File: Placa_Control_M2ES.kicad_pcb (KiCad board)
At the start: 2 copper layers, 204 x 108 mm, 311 parts, among them J1 Screw_Terminal_01x06, J10 Screw_Terminal_01x06, J11 Screw_Terminal_01x02, J12 7499010211A, J13 Screw_Terminal_01x04, J2 Screw_Terminal_01x06, J3 Screw_Terminal_01x06, J4 Screw_Terminal_01x06, J5 Screw_Terminal_01x06, J6 Screw_Terminal_01x06, J7 Screw_Terminal_01x06, J8 Screw_Terminal_01x06, J9 Screw_Terminal_01x06, K1 HF46F-G, K10 HF46F-G, K11 HF46F-G, K12 HF46F-G, K2 HF46F-G, K3 HF46F-G, K4 HF46F-G, K5 HF46F-G, K6 HF46F-G, K7 HF46F-G, K8 HF46F-G, K9 HF46F-G, U1 ULN2003, U10 L78M08CDT-TR, U11 LD29150, U12 LAN8742A, U13 USBLC6-4SC6, U14 TLV9101, U15 TLV9101, U16 TLV9101, U17 TLV9101, U18 TLV9101, U19 TLV9101, U2 ULN2003, U20 TLV9101, U21 TLV9101, U22 REF3030, U23 STM32H743VITx, U3 REF35102QDBVR, U4 ADS1256, U5 ADS1256, U6 TLV9101, U7 OKI-78SR-12_1.0-W36-C, U8 uA7810, U9 LD29150, Y1 8.0Mhz, Y2 8.0Mhz, Y3 25Mhz, Y4 8Mhz

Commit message: Avance del posicionamiento
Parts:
- removed J7: Screw_Terminal_01x06, LIB_PCB_CONT:15EDGVC_6P_3.81mm_Male-Vert_Degson
- moved R60 283.1 mm to (242.6, 83.1), turned to 180 degrees
- moved R61 281.1 mm to (242.6, 81.5), turned to 0 degrees
- moved D3 278.6 mm to (237.5, 82.2), turned to 0 degrees
- moved C66 277.4 mm to (233.4, 79.8), turned to 180 degrees
- moved R64 271.2 mm to (240.2, 82.3), turned to -90 degrees
- moved U14 270.8 mm to (233.4, 82.1), turned to 0 degrees
- moved R62 267.2 mm to (230.5, 80.5), turned to -90 degrees
- moved R63 263.9 mm to (230.5, 83.7)
- moved D4 262.8 mm to (228.7, 83.8), turned to -90 degrees
- moved R65 261.5 mm to (233.2, 84.4), turned to 0 degrees
- moved R66 255.8 mm to (228.7, 80.6), turned to -90 degrees
- moved C13 193.3 mm to (170.7, 54.7)
- moved C14 189.3 mm to (171.8, 59.1), turned to 0 degrees
- moved U4 177.7 mm to (164.0, 57.6), turned to -90 degrees
- moved C9 177.3 mm to (157.2, 60.5)
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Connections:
- J5 pad 2: /Digital Inputs/NAMUR_1 -> /8V
- J5 pad 3: /8V -> GND
- J5 pad 4: /Digital Inputs/NAMUR_2 -> /Digital Inputs/NAMUR_1
- J5 pad 5: /8V -> /Digital Inputs/NAMUR_2
- J6 pad 1: /8V -> /Digital Inputs/NAMUR_4
- J6 pad 2: /Digital Inputs/NAMUR_4 -> /Digital Inputs/NAMUR_5
- J6 pad 3: /8V -> /Digital Inputs/NAMUR_6
- J6 pad 4: /Digital Inputs/NAMUR_5 -> /Digital Inputs/NAMUR_7
- J6 pad 5: /8V -> /Digital Inputs/NAMUR_8
- J6 pad 6: /Digital Inputs/NAMUR_6 -> /Digital Inputs/NAMUR_9

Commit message: Se empieza a evaluar la conexión del ethernet con la carcasa, parte analog, dig y micro en posición, tambien se busca solución para la salida de led de las entradas digitales
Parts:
- removed C74: 100nF/50V, Capacitor_SMD:C_0603_1608Metric
- removed J12: 7499010211A, Connector_RJ:RJ45_Wuerth_7499010211A_Horizontal
- added J7: ARJM11C7-009-AB-EW2, LIB_PCB_CONT:ARJM11C7-009-AB-EW2_Abracon, F.Cu at (238.5, 44.1)
- C57: value 10uF/50V -> 1uF/50V
- C60: value 10nF/50V -> 100nF/50V
- moved R74 299.0 mm to (242.3, 104.5), turned to 180 degrees
- moved D15 298.1 mm to (239.0, 125.8), turned to -90 degrees
- moved D7 297.2 mm to (239.1, 104.1), turned to -90 degrees
- moved R106 297.0 mm to (242.4, 127.8), turned to 0 degrees
- moved R102 297.0 mm to (242.4, 126.2)
- moved R103 297.0 mm to (242.4, 124.6), turned to 0 degrees
- moved R75 296.5 mm to (242.3, 102.9), turned to 0 degrees
- moved U20 294.6 mm to (235.8, 125.6), turned to 90 degrees
- moved C68 292.9 mm to (233.7, 103.6), turned to -90 degrees
- moved D16 291.4 mm to (232.8, 127.8)
- moved U16 289.9 mm to (235.9, 103.9)
- moved D5 289.1 mm to (239.1, 98.7), turned to -90 degrees
- moved R78 289.0 mm to (242.3, 106.1), turned to 0 degrees
- moved C72 288.3 mm to (233.6, 125.3), turned to -90 degrees
- moved R67 287.7 mm to (242.3, 99.0)
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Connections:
- J5 pad 1: /8V -> /Digital Inputs/NAMUR_6
- J5 pad 2: /8V -> /Digital Inputs/NAMUR_5
- J5 pad 3: GND -> /Digital Inputs/NAMUR_4
- J5 pad 4: /Digital Inputs/NAMUR_1 -> /Digital Inputs/NAMUR_3
- J5 pad 6: /Digital Inputs/NAMUR_3 -> /Digital Inputs/NAMUR_1
- J6 pad 1: /Digital Inputs/NAMUR_4 -> /8V
- J6 pad 2: /Digital Inputs/NAMUR_5 -> GND
- J6 pad 3: /Digital Inputs/NAMUR_6 -> unconnected-(J6-Pin_3-Pad3)
- J6 pad 4: /Digital Inputs/NAMUR_7 -> /Digital Inputs/NAMUR_9
- J6 pad 6: /Digital Inputs/NAMUR_9 -> /Digital Inputs/NAMUR_7
- U23 pad 1: /Digital Inputs/DIG_9 -> unconnected-(U23-PE2-Pad1)
- U23 pad 46: unconnected-(U23-PB10-Pad46) -> /Analog Inputs/ADS_SCLK
- U23 pad 53: unconnected-(U23-PB14-Pad53) -> /Analog Inputs/ADS_MISO
- U23 pad 54: unconnected-(U23-PB15-Pad54) -> /Analog Inputs/ADS_MOSI
- U23 pad 55: unconnected-(U23-PD8-Pad55) -> /Analog Inputs/ADS2_DRDY
- U23 pad 56: unconnected-(U23-PD9-Pad56) -> /Analog Inputs/ADS2_CS
- U23 pad 57: unconnected-(U23-PD10-Pad57) -> /Analog Inputs/ADS1_DRDY
- U23 pad 58: unconnected-(U23-PD11-Pad58) -> /Analog Inputs/ADS1_CS
- U23 pad 60: /Digital Outputs/Relay_1 -> /Digital Outputs/Relay_12
- U23 pad 61: /Digital Outputs/Relay_2 -> /Digital Outputs/Relay_11
- U23 pad 62: /Digital Outputs/Relay_3 -> /Digital Outputs/Relay_10
- U23 pad 63: /Digital Outputs/Relay_4 -> /Digital Outputs/Relay_9
- U23 pad 64: /Digital Outputs/Relay_5 -> /Digital Outputs/Relay_8
- U23 pad 65: /Digital Outputs/Relay_6 -> /Digital Outputs/Relay_7
- U23 pad 66: /Digital Outputs/Relay_7 -> /Digital Outputs/Relay_6
- U23 pad 67: /Digital Outputs/Relay_8 -> /Digital Outputs/Relay_5
- U23 pad 68: /Digital Outputs/Relay_9 -> /Digital Outputs/Relay_4
- U23 pad 69: /Digital Outputs/Relay_10 -> /Digital Outputs/Relay_3
- U23 pad 70: /Digital Outputs/Relay_11 -> /Digital Outputs/Relay_2
- U23 pad 71: /Digital Outputs/Relay_12 -> /Digital Outputs/Relay_1
- U23 pad 78: /Analog Inputs/ADS_SCLK -> unconnected-(U23-PC10-Pad78)
- U23 pad 79: /Analog Inputs/ADS_MISO -> unconnected-(U23-PC11-Pad79)
- U23 pad 80: /Analog Inputs/ADS_MOSI -> unconnected-(U23-PC12-Pad80)
- U23 pad 83: /Analog Inputs/ADS1_DRDY -> unconnected-(U23-PD2-Pad83)
- U23 pad 84: /Analog Inputs/ADS1_CS -> /Digital Inputs/DIG_9
- U23 pad 85: /Analog Inputs/ADS2_DRDY -> /Digital Inputs/DIG_8
- U23 pad 86: /Analog Inputs/ADS2_CS -> /Digital Inputs/DIG_7
- U23 pad 87: unconnected-(U23-PD6-Pad87) -> /Digital Inputs/DIG_6
- U23 pad 90: /Digital Inputs/DIG_1 -> /Digital Inputs/DIG_5
- U23 pad 91: /Digital Inputs/DIG_2 -> /Digital Inputs/DIG_4
- U23 pad 93: /Digital Inputs/DIG_4 -> unconnected-(U23-PB7-Pad93)
- U23 pad 95: /Digital Inputs/DIG_5 -> unconnected-(U23-PB8-Pad95)
- U23 pad 96: /Digital Inputs/DIG_6 -> /Digital Inputs/DIG_2
- U23 pad 97: /Digital Inputs/DIG_7 -> /Digital Inputs/DIG_1
- U23 pad 98: /Digital Inputs/DIG_8 -> unconnected-(U23-PE1-Pad98)
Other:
- outline, holes or cut-outs redrawn

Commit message: Se traza vcc, digital, analog, relay, esta por terminar corregir GND y revisar nuevamente
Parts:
- removed D10, D12, D14, D16, D18, D2, D4, D6, D8: LED, LED_SMD:LED_0603_1608Metric
- removed R101, R108, R115, R66, R73, R80, R87, R9, R94: 2k2, Resistor_SMD:R_0603_1608Metric
- moved J13 139.4 mm to (177.3, 91.1)
- moved JP1 105.1 mm to (211.2, 75.9), turned to 180 degrees
- moved C76 90.9 mm to (211.3, 78.2), turned to 0 degrees
- moved C53 82.9 mm to (230.3, 78.4), turned to 180 degrees
- moved FB1 75.5 mm to (226.5, 65.9), turned to 180 degrees
- moved C55 58.6 mm to (230.5, 76.6), turned to 180 degrees
- moved C56 57.5 mm to (235.9, 75.7), turned to -90 degrees
- moved R47 18.8 mm to (202.1, 63.2), turned to 180 degrees
- moved C5 18.6 mm to (87.7, 66.6), turned to 90 degrees
- moved R39 18.3 mm to (190.6, 61.9)
- moved R44 18.3 mm to (189.0, 61.9)
- moved R55 17.9 mm to (229.3, 58.3), turned to 180 degrees
- moved R41 17.2 mm to (202.1, 64.9), turned to 0 degrees
- moved R45 16.5 mm to (202.1, 66.5), turned to 180 degrees
- moved R40 16.4 mm to (197.8, 61.9)
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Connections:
- C20 pad 1: Net-(PS1-AC/L) -> Net-(J11-Pin_1)
- C20 pad 2: Net-(J11-Pin_2) -> Net-(PS1-AC/N)
- F1 pad 1: Net-(J11-Pin_1) -> Net-(J11-Pin_2)
- F1 pad 2: Net-(PS1-AC/L) -> Net-(PS1-AC/N)
- J7 pad S1: Net-(J7-PadS1) -> unconnected-(J7-PadS1)_1
- J7 pad S2: Net-(J7-PadS1) -> unconnected-(J7-PadS1)
- PS1 pad 1: Net-(J11-Pin_2) -> Net-(PS1-AC/N)
- PS1 pad 2: Net-(PS1-AC/L) -> Net-(J11-Pin_1)
- RV1 pad 1: Net-(PS1-AC/L) -> Net-(J11-Pin_1)
- RV1 pad 2: Net-(J11-Pin_2) -> Net-(PS1-AC/N)
- U23 pad 55: /Analog Inputs/ADS2_DRDY -> /Analog Inputs/ADS1_DRDY
- U23 pad 56: /Analog Inputs/ADS2_CS -> /Analog Inputs/ADS1_CS
- U23 pad 57: /Analog Inputs/ADS1_DRDY -> /Analog Inputs/ADS2_DRDY
- U23 pad 58: /Analog Inputs/ADS1_CS -> /Analog Inputs/ADS2_CS
- U23 pad 81: unconnected-(U23-PD0-Pad81) -> /Digital Inputs/DIG_9
- U23 pad 82: unconnected-(U23-PD1-Pad82) -> /Digital Inputs/DIG_8
- U23 pad 83: unconnected-(U23-PD2-Pad83) -> /Digital Inputs/DIG_7
- U23 pad 84: /Digital Inputs/DIG_9 -> /Digital Inputs/DIG_6
- U23 pad 85: /Digital Inputs/DIG_8 -> unconnected-(U23-PD4-Pad85)
- U23 pad 86: /Digital Inputs/DIG_7 -> unconnected-(U23-PD5-Pad86)
- U23 pad 87: /Digital Inputs/DIG_6 -> unconnected-(U23-PD6-Pad87)
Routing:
- net /3V3: track 0.00 -> 541.4 mm, vias 0 -> 33
- net /24V: track 0.00 -> 335.9 mm
- net /8V: track 0.00 -> 188.1 mm, vias 0 -> 4
- net /5V: track 0.00 -> 154.1 mm, vias 0 -> 3
- net GND: track 0.00 -> 134.0 mm, vias 0 -> 53
- net /Ethernet/ETH_TXD1: track 0.00 -> 128.7 mm, vias 0 -> 2
- net /Ethernet/ETH_TXD0: track 0.00 -> 123.6 mm, vias 0 -> 2
- net /10V: track 0.00 -> 107.2 mm
- net /Ethernet/ETH_TX_EN: track 0.00 -> 106.3 mm, vias 0 -> 2
- net /Digital Inputs/DIG_9: track 0.00 -> 91.8 mm
- net /Fuente/12V: track 0.00 -> 91.7 mm
- net /Digital Inputs/DIG_8: track 0.00 -> 86.8 mm
- net /Analog Inputs/REF_2.5V: track 0.00 -> 85.7 mm, vias 0 -> 3
- net /Digital Inputs/DIG_7: track 0.00 -> 80.7 mm
- net /Ethernet/ETH_MDIO: track 0.00 -> 80.6 mm
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- added copper zone on B.Cu, net GND
- added copper zone on F.Cu, net GND
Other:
- outline, holes or cut-outs redrawn

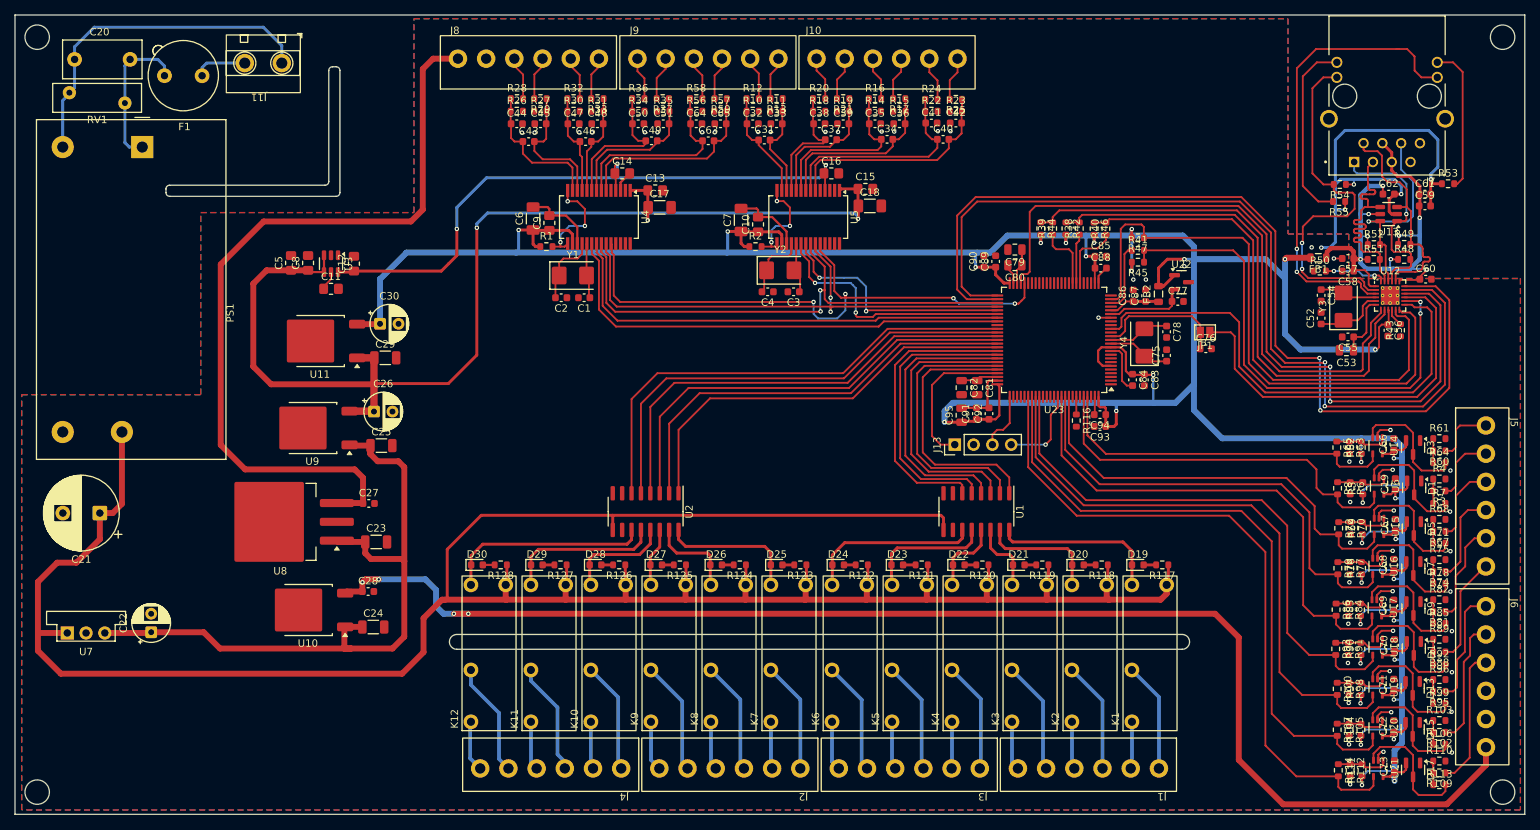
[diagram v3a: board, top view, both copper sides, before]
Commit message: Se termina de revisar la placa. Se corrige la terminación de los transformadores internos del puerto ethernet. Se revisa GND, espaciado, añadimos notas. Falta enlazar las partes de JLCPCN
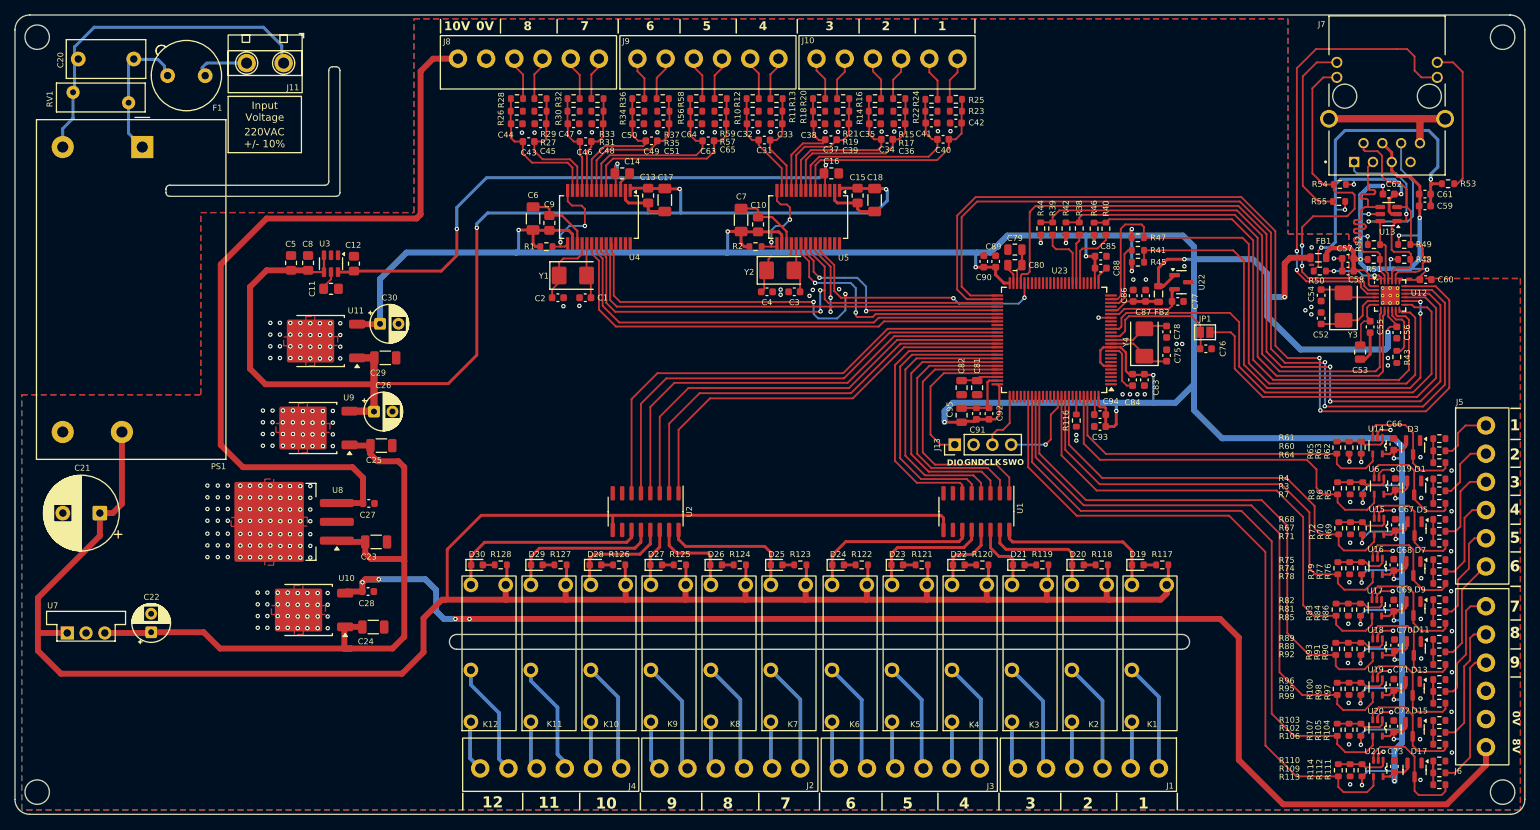
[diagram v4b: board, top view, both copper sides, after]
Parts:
- moved R43 3.63 mm to (237.1, 79.3)
- moved C55 3.29 mm to (233.5, 75.2), turned to -90 degrees
- moved C53 1.87 mm to (232.1, 78.6), turned to -90 degrees
- moved C15 1.38 mm to (164.2, 57.5), turned to -90 degrees
- moved C56 1.24 mm to (237.1, 76.0)
- moved C17 1.22 mm to (138.2, 58.1), turned to -90 degrees
- moved C13 1.18 mm to (135.9, 57.5), turned to -90 degrees
- moved C18 1.03 mm to (166.5, 58.1), turned to -90 degrees
- moved C20 0.50 mm to (58.9, 39.0)
- moved RV1 0.50 mm to (58.2, 43.5)
- moved C2 0.45 mm to (123.7, 71.3)
- moved F1 0.42 mm to (76.1, 41.3)
- moved J11 0.25 mm to (89.2, 35.8)
- moved D17 0.20 mm to (239.5, 135.1)
- moved C1 0.15 mm to (127.4, 71.3)
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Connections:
- C31 pad 1: /Analog Inputs/IN3_P -> /Analog Inputs/IN4_P
- C31 pad 2: /Analog Inputs/IN3_N -> /Analog Inputs/IN4_N
- C32 pad 1: /Analog Inputs/IN3_P -> /Analog Inputs/IN4_P
- C33 pad 2: /Analog Inputs/IN3_N -> /Analog Inputs/IN4_N
- C34 pad 1: /Analog Inputs/IN1_P -> /Analog Inputs/IN2_P
- C34 pad 2: /Analog Inputs/IN1_N -> /Analog Inputs/IN2_N
- C35 pad 1: /Analog Inputs/IN1_P -> /Analog Inputs/IN2_P
- C36 pad 2: /Analog Inputs/IN1_N -> /Analog Inputs/IN2_N
- C37 pad 1: /Analog Inputs/IN2_P -> /Analog Inputs/IN3_P
- C37 pad 2: /Analog Inputs/IN2_N -> /Analog Inputs/IN3_N
- C38 pad 1: /Analog Inputs/IN2_P -> /Analog Inputs/IN3_P
- C39 pad 2: /Analog Inputs/IN2_N -> /Analog Inputs/IN3_N
- C40 pad 1: /Analog Inputs/IN0_P -> /Analog Inputs/IN1_P
- C40 pad 2: /Analog Inputs/IN0_N -> /Analog Inputs/IN1_N
- C41 pad 1: /Analog Inputs/IN0_P -> /Analog Inputs/IN1_P
- C42 pad 2: /Analog Inputs/IN0_N -> /Analog Inputs/IN1_N
- C43 pad 1: /Analog Inputs/IN7_P -> /Analog Inputs/IN8_P
- C43 pad 2: /Analog Inputs/IN7_N -> /Analog Inputs/IN8_N
- C44 pad 1: /Analog Inputs/IN7_P -> /Analog Inputs/IN8_P
- C45 pad 2: /Analog Inputs/IN7_N -> /Analog Inputs/IN8_N
- C46 pad 1: /Analog Inputs/IN6_P -> /Analog Inputs/IN7_P
- C46 pad 2: /Analog Inputs/IN6_N -> /Analog Inputs/IN7_N
- C47 pad 1: /Analog Inputs/IN6_P -> /Analog Inputs/IN7_P
- C48 pad 2: /Analog Inputs/IN6_N -> /Analog Inputs/IN7_N
- C49 pad 1: /Analog Inputs/IN5_P -> /Analog Inputs/IN6_P
- C49 pad 2: /Analog Inputs/IN5_N -> /Analog Inputs/IN6_N
- C50 pad 1: /Analog Inputs/IN5_P -> /Analog Inputs/IN6_P
- C51 pad 2: /Analog Inputs/IN5_N -> /Analog Inputs/IN6_N
- C63 pad 1: /Analog Inputs/IN4_P -> /Analog Inputs/IN5_P
- C63 pad 2: /Analog Inputs/IN4_N -> /Analog Inputs/IN5_N
- C64 pad 1: /Analog Inputs/IN4_P -> /Analog Inputs/IN5_P
- C65 pad 2: /Analog Inputs/IN4_N -> /Analog Inputs/IN5_N
- J10 pad 1: /Analog Inputs/SENS0_B -> /Analog Inputs/SENS1_B
- J10 pad 2: /Analog Inputs/SENS0_A -> /Analog Inputs/SENS1_A
- J10 pad 3: /Analog Inputs/SENS1_B -> /Analog Inputs/SENS2_B
- J10 pad 4: /Analog Inputs/SENS1_A -> /Analog Inputs/SENS2_A
- J10 pad 5: /Analog Inputs/SENS2_B -> /Analog Inputs/SENS3_B
- J10 pad 6: /Analog Inputs/SENS2_A -> /Analog Inputs/SENS3_A
- J7 pad S1: unconnected-(J7-PadS1)_1 -> GNDPWR
- J7 pad S2: unconnected-(J7-PadS1) -> GNDPWR
- J8 pad 1: /Analog Inputs/SENS6_B -> /Analog Inputs/SENS7_B
- J8 pad 2: /Analog Inputs/SENS6_A -> /Analog Inputs/SENS7_A
- J8 pad 3: /Analog Inputs/SENS7_B -> /Analog Inputs/SENS8_B
- J8 pad 4: /Analog Inputs/SENS7_A -> /Analog Inputs/SENS8_A
- J9 pad 1: /Analog Inputs/SENS3_B -> /Analog Inputs/SENS4_B
- J9 pad 2: /Analog Inputs/SENS3_A -> /Analog Inputs/SENS4_A
- J9 pad 3: /Analog Inputs/SENS4_B -> /Analog Inputs/SENS5_B
- J9 pad 4: /Analog Inputs/SENS4_A -> /Analog Inputs/SENS5_A
- J9 pad 5: /Analog Inputs/SENS5_B -> /Analog Inputs/SENS6_B
- J9 pad 6: /Analog Inputs/SENS5_A -> /Analog Inputs/SENS6_A
- R10 pad 1: /Analog Inputs/IN3_P -> /Analog Inputs/IN4_P
- R11 pad 2: /Analog Inputs/IN3_N -> /Analog Inputs/IN4_N
- R12 pad 1: /Analog Inputs/IN3_P -> /Analog Inputs/IN4_P
- R12 pad 2: /Analog Inputs/SENS3_A -> /Analog Inputs/SENS4_A
- R13 pad 1: /Analog Inputs/IN3_N -> /Analog Inputs/IN4_N
- R13 pad 2: /Analog Inputs/SENS3_B -> /Analog Inputs/SENS4_B
- R14 pad 1: /Analog Inputs/IN1_P -> /Analog Inputs/IN2_P
- R15 pad 2: /Analog Inputs/IN1_N -> /Analog Inputs/IN2_N
- R16 pad 1: /Analog Inputs/IN1_P -> /Analog Inputs/IN2_P
- R16 pad 2: /Analog Inputs/SENS1_A -> /Analog Inputs/SENS2_A
- R17 pad 1: /Analog Inputs/IN1_N -> /Analog Inputs/IN2_N
- R17 pad 2: /Analog Inputs/SENS1_B -> /Analog Inputs/SENS2_B
- R18 pad 1: /Analog Inputs/IN2_P -> /Analog Inputs/IN3_P
- R19 pad 2: /Analog Inputs/IN2_N -> /Analog Inputs/IN3_N
- R20 pad 1: /Analog Inputs/IN2_P -> /Analog Inputs/IN3_P
- R20 pad 2: /Analog Inputs/SENS2_A -> /Analog Inputs/SENS3_A
- R21 pad 1: /Analog Inputs/IN2_N -> /Analog Inputs/IN3_N
- R21 pad 2: /Analog Inputs/SENS2_B -> /Analog Inputs/SENS3_B
- R22 pad 1: /Analog Inputs/IN0_P -> /Analog Inputs/IN1_P
- R23 pad 2: /Analog Inputs/IN0_N -> /Analog Inputs/IN1_N
- R24 pad 1: /Analog Inputs/IN0_P -> /Analog Inputs/IN1_P
- R24 pad 2: /Analog Inputs/SENS0_A -> /Analog Inputs/SENS1_A
- R25 pad 1: /Analog Inputs/IN0_N -> /Analog Inputs/IN1_N
- R25 pad 2: /Analog Inputs/SENS0_B -> /Analog Inputs/SENS1_B
- R26 pad 1: /Analog Inputs/IN7_P -> /Analog Inputs/IN8_P
- R27 pad 2: /Analog Inputs/IN7_N -> /Analog Inputs/IN8_N
- R28 pad 1: /Analog Inputs/IN7_P -> /Analog Inputs/IN8_P
- R28 pad 2: /Analog Inputs/SENS7_A -> /Analog Inputs/SENS8_A
- R29 pad 1: /Analog Inputs/IN7_N -> /Analog Inputs/IN8_N
- R29 pad 2: /Analog Inputs/SENS7_B -> /Analog Inputs/SENS8_B
- R30 pad 1: /Analog Inputs/IN6_P -> /Analog Inputs/IN7_P
- R31 pad 2: /Analog Inputs/IN6_N -> /Analog Inputs/IN7_N
- R32 pad 1: /Analog Inputs/IN6_P -> /Analog Inputs/IN7_P
- R32 pad 2: /Analog Inputs/SENS6_A -> /Analog Inputs/SENS7_A
- R33 pad 1: /Analog Inputs/IN6_N -> /Analog Inputs/IN7_N
- R33 pad 2: /Analog Inputs/SENS6_B -> /Analog Inputs/SENS7_B
- R34 pad 1: /Analog Inputs/IN5_P -> /Analog Inputs/IN6_P
- R35 pad 2: /Analog Inputs/IN5_N -> /Analog Inputs/IN6_N
- R36 pad 1: /Analog Inputs/IN5_P -> /Analog Inputs/IN6_P
- R36 pad 2: /Analog Inputs/SENS5_A -> /Analog Inputs/SENS6_A
- R37 pad 1: /Analog Inputs/IN5_N -> /Analog Inputs/IN6_N
- R37 pad 2: /Analog Inputs/SENS5_B -> /Analog Inputs/SENS6_B
- R56 pad 1: /Analog Inputs/IN4_P -> /Analog Inputs/IN5_P
- R57 pad 2: /Analog Inputs/IN4_N -> /Analog Inputs/IN5_N
- R58 pad 1: /Analog Inputs/IN4_P -> /Analog Inputs/IN5_P
- R58 pad 2: /Analog Inputs/SENS4_A -> /Analog Inputs/SENS5_A
- R59 pad 1: /Analog Inputs/IN4_N -> /Analog Inputs/IN5_N
- R59 pad 2: /Analog Inputs/SENS4_B -> /Analog Inputs/SENS5_B
- U4 pad 10: /Analog Inputs/IN6_N -> /Analog Inputs/IN7_N
- U4 pad 11: /Analog Inputs/IN6_P -> /Analog Inputs/IN7_P
- U4 pad 12: /Analog Inputs/IN7_N -> /Analog Inputs/IN8_N
- U4 pad 13: /Analog Inputs/IN7_P -> /Analog Inputs/IN8_P
- U4 pad 6: /Analog Inputs/IN4_N -> /Analog Inputs/IN5_N
- U4 pad 7: /Analog Inputs/IN4_P -> /Analog Inputs/IN5_P
- U4 pad 8: /Analog Inputs/IN5_N -> /Analog Inputs/IN6_N
- U4 pad 9: /Analog Inputs/IN5_P -> /Analog Inputs/IN6_P
- U5 pad 10: /Analog Inputs/IN2_N -> /Analog Inputs/IN3_N
- U5 pad 11: /Analog Inputs/IN2_P -> /Analog Inputs/IN3_P
- U5 pad 12: /Analog Inputs/IN3_N -> /Analog Inputs/IN4_N
- U5 pad 13: /Analog Inputs/IN3_P -> /Analog Inputs/IN4_P
- U5 pad 6: /Analog Inputs/IN0_N -> /Analog Inputs/IN1_N
- U5 pad 7: /Analog Inputs/IN0_P -> /Analog Inputs/IN1_P
- U5 pad 8: /Analog Inputs/IN1_N -> /Analog Inputs/IN2_N
- U5 pad 9: /Analog Inputs/IN1_P -> /Analog Inputs/IN2_P
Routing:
- net /Analog Inputs/IN0_N: track 30.3 -> 0.00 mm
- net /Analog Inputs/IN0_P: track 29.2 -> 0.00 mm
- net GND: track 134.0 -> 160.2 mm, vias 53 -> 255
- net /Analog Inputs/IN8_P: track 0.00 -> 19.3 mm
- net GNDPWR: track 0.00 -> 19.0 mm
- net /Analog Inputs/IN8_N: track 0.00 -> 18.4 mm
- net /Analog Inputs/IN4_N: track 27.1 -> 14.5 mm
- net /Analog Inputs/IN4_P: track 26.1 -> 14.9 mm
- net /5V: track 154.1 -> 163.2 mm
- net /Analog Inputs/IN5_N: track 20.4 -> 27.1 mm
- net /Analog Inputs/IN6_N: track 13.9 -> 20.4 mm
- net /Analog Inputs/IN5_P: track 19.8 -> 26.1 mm
- net /Analog Inputs/IN2_N: track 18.0 -> 24.3 mm
- net /Analog Inputs/IN2_P: track 17.2 -> 23.4 mm
- net /Analog Inputs/IN1_N: track 24.3 -> 30.3 mm
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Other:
- outline, holes or cut-outs redrawn
- board text added: "0V"
- board text added: "1"
- board text added: "10"
- board text added: "10V"
- board text added: "11"
- board text added: "12"
- board text added: "2"
- board text added: "220VAC +/- 10%"
- board text added: "3"
- board text added: "4"
- board text added: "5"
- board text added: "6"
- board text added: "7"
- board text added: "8"
- board text added: "8V"
- board text added: "9"
- board text added: "CLK"
- board text added: "DIO"
- board text added: "GND"
- board text added: "Input Voltage"
- board text added: "SWO"
